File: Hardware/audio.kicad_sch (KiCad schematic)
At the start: 35 parts, among them J13 ANT_BNC, J14 ANT_BNC, J15 Audio IN, Q3 MMBT2222A, U10 Si4732, U9 LM358, X1 Q13FC1350000400

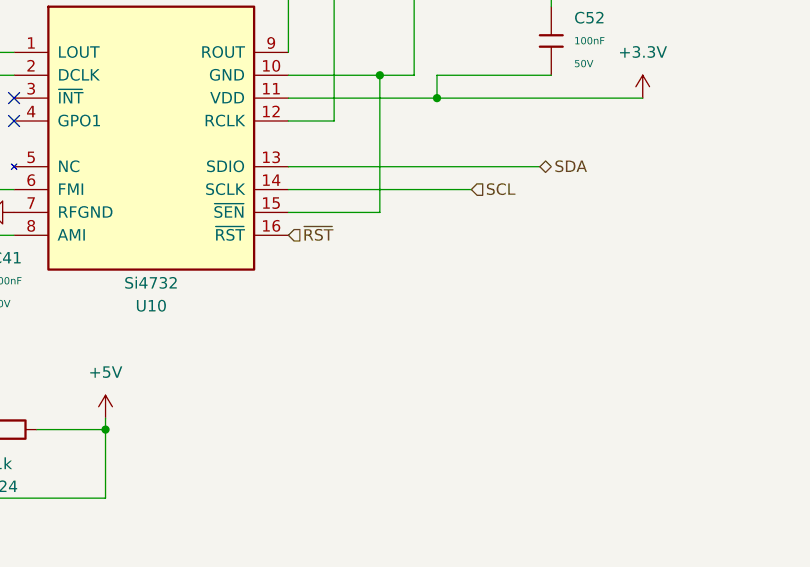
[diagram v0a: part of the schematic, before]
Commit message: Hardware errors found.
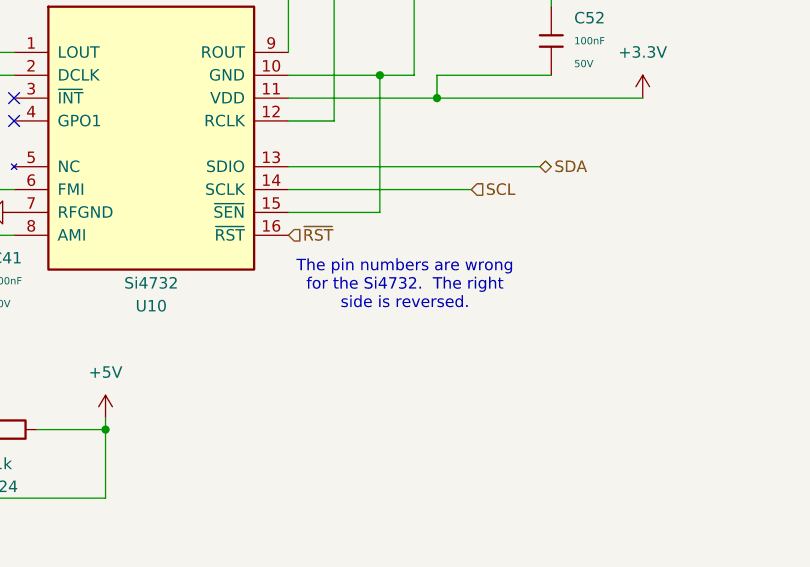
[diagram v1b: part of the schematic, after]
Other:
- note added: "The pin numbers are wrong for the Si4732. The right side is reversed."
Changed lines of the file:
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@@
 	(generator_version "9.0")
 	(paper "A4")
+	(text "The pin numbers are wrong\nfor the Si4732.  The right\nside is reversed."
+		(exclude_from_sim no)
+		(at 119.634 133.858 0)
+		(effects
+			(font
+				(face "KiCad Font")
+				(size 1.27 1.27)
+			)
+		)
+	)
 	(junction
 		(at 121.92 62.23)
